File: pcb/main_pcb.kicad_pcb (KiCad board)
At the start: 2 copper layers, 62 x 67 mm, 30 parts, among them J1 Conn_01x06_Socket, J2 Conn_01x10_Pin, J3 Conn_01x06_Pin, J4 USB_C_Receptacle_USB2.0, SW1 SW_Push, SW2 SW_Push, SW3 SW_Push, U1 ESP32-H2-MINI-1, U2 LM5165Y

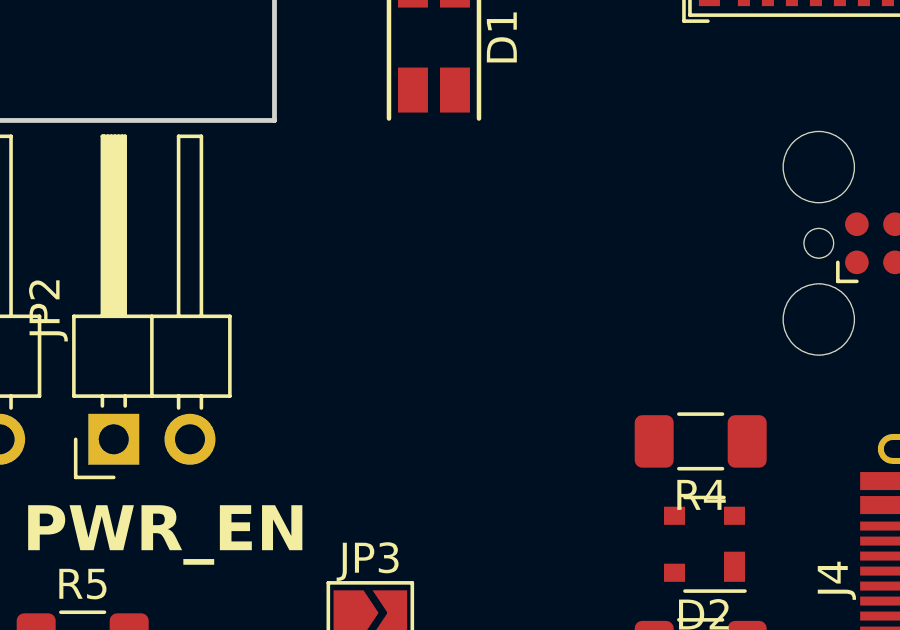
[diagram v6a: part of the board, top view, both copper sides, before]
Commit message: Improve USB circuit
Add reverse voltage protection and VBUS capacitor.
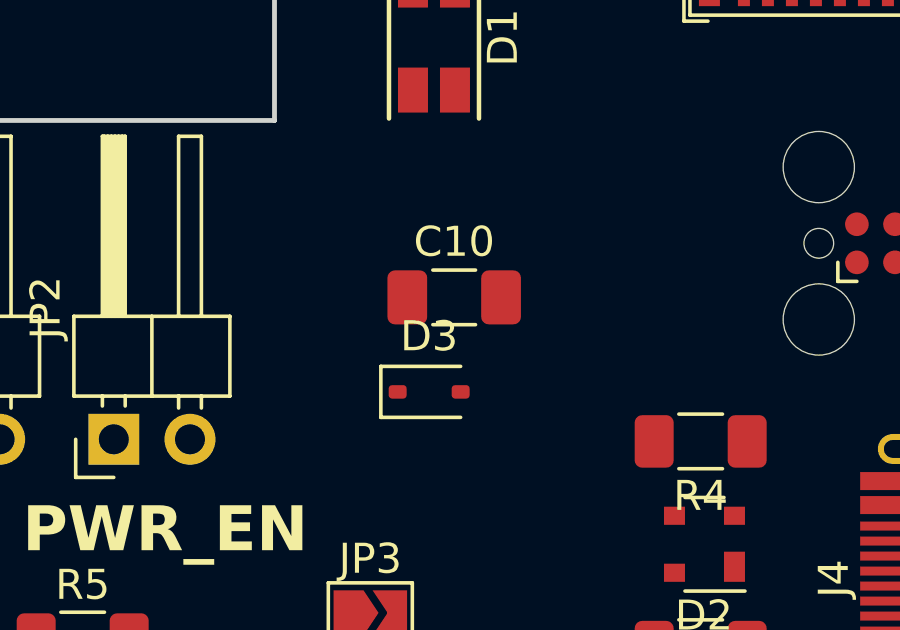
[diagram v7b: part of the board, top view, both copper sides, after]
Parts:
- added C10: 10uF, Capacitor_SMD:C_1206_3216Metric_Pad1.33x1.80mm_HandSolder, F.Cu at (148.5, 70.1)
- added D3: 1N5819WS, Diode_SMD:D_SOD-323, F.Cu at (147.7, 73.3)
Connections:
- JP3 pad 2: VDD -> Net-(D3-A)
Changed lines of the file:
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@@
   (net 59 "unconnected-(U1-GPIO12-Pad16)")
   (net 60 "Net-(R6-Pad2)")
+  (net 61 "unconnected-(C10-Pad2)")
+  (net 62 "Net-(D3-A)")
   (footprint "Button_Switch_SMD:SW_SPST_PTS645" (layer "F.Cu")
     (at 165.227 98.679)
@@
       ))
     (pad "2" smd custom (at 0.725 0) (size 0.3 0.3) (layers "F.Cu" "F.Mask")
-      (net 29 "VDD") (pinfunction "B") (pintype "passive") (zone_connect 2)
+      (net 62 "Net-(D3-A)") (pinfunction "B") (pintype "passive") (zone_connect 2)
       (options (clearance outline) (anchor rect))
       (primitives
@@
   )
   (footprint "Capacitor_SMD:C_1206_3216Metric_Pad1.33x1.80mm_HandSolder" (layer "F.Cu")
+    (at 148.502 70.129)
+    (descr "Capacitor SMD 1206 (3216 Metric), square (rectangular) end terminal, IPC_7351 nominal with elongated pad for handsoldering. (Body size source: IPC-SM-782 page 76, https://www.pcb-3d.com/wordpress/wp-content/uploads/ipc-sm-782a_amendment_1_and_2.pdf), generated with kicad-footprint-generator")
+    (tags "capacitor handsolder")
+    (property "Sheetfile" "main_pcb.kicad_sch")
+    (property "Sheetname" "")
+    (property "ki_description" "Unpolarized capacitor")
+    (property "ki_keywords" "cap capacitor")
+    (attr smd)
+    (fp_text reference "C10" (at 0 -1.85) (layer "F.SilkS")
+        (effects (font (size 1 1) (thickness 0.15)))
+    )
+    (fp_text value "10uF" (at 0 1.85) (layer "F.Fab")
+        (effects (font (size 1 1) (thickness 0.15)))
+    )
+    (fp_text user "${REFERENCE}" (at 0 0) (layer "F.Fab")
+        (effects (font (size 0.8 0.8) (thickness 0.12)))
+    )
+    (fp_line (start -0.711252 -0.91) (end 0.711252 -0.91)
+      (stroke (width 0.12) (type solid)) (layer "F.SilkS"))
+    (fp_line (start -0.711252 0.91) (end 0.711252 0.91)
+      (stroke (width 0.12) (type solid)) (layer "F.SilkS"))
+    (fp_line (start -2.48 -1.15) (end 2.48 -1.15)
+      (stroke (width 0.05) (type solid)) (layer "F.CrtYd"))
+    (fp_line (start -2.48 1.15) (end -2.48 -1.15)
+      (stroke (width 0.05) (type solid)) (layer "F.CrtYd"))
+    (fp_line (start 2.48 -1.15) (end 2.48 1.15)
+      (stroke (width 0.05) (type solid)) (layer "F.CrtYd"))
+    (fp_line (start 2.48 1.15) (end -2.48 1.15)
+      (stroke (width 0.05) (type solid)) (layer "F.CrtYd"))
+    (fp_line (start -1.6 -0.8) (end 1.6 -0.8)
+      (stroke (width 0.1) (type solid)) (layer "F.Fab"))
+    (fp_line (start -1.6 0.8) (end -1.6 -0.8)
+      (stroke (width 0.1) (type solid)) (layer "F.Fab"))
+    (fp_line (start 1.6 -0.8) (end 1.6 0.8)
+      (stroke (width 0.1) (type solid)) (layer "F.Fab"))
+    (fp_line (start 1.6 0.8) (end -1.6 0.8)
+      (stroke (width 0.1) (type solid)) (layer "F.Fab"))
+    (pad "1" smd roundrect (at -1.5625 0) (size 1.325 1.8) (layers "F.Cu" "F.Paste" "F.Mask") (roundrect_rratio 0.188679)
+      (net 29 "VDD") (pintype "passive"))
+    (pad "2" smd roundrect (at 1.5625 0) (size 1.325 1.8) (layers "F.Cu" "F.Paste" "F.Mask") (roundrect_rratio 0.188679)
+      (net 61 "unconnected-(C10-Pad2)") (pintype "passive"))
+    (model "${KICAD6_3DMODEL_DIR}/Capacitor_SMD.3dshapes/C_1206_3216Metric.wrl"
+      (offset (xyz 0 0 0))
+      (scale (xyz 1 1 1))
+      (rotate (xyz 0 0 0))
+    )
+  )
+  (footprint "Capacitor_SMD:C_1206_3216Metric_Pad1.33x1.80mm_HandSolder" (layer "F.Cu")
     (at 130.556 80.264)
     (descr "Capacitor SMD 1206 (3216 Metric), square (rectangular) end terminal, IPC_7351 nominal with elongated pad for handsoldering. (Body size source: IPC-SM-782 page 76, https://www.pcb-3d.com/wordpress/wp-content/uploads/ipc-sm-782a_amendment_1_and_2.pdf), generated with kicad-footprint-generator")
@@
       (offset (xyz 0 0 0))
       (scale (xyz 1 1 1))
+      (rotate (xyz 0 0 0))
+    )
+  )
+  (footprint "Diode_SMD:D_SOD-323" (layer "F.Cu")
+    (at 147.667 73.279)
+    (descr "SOD-323")
+    (tags "SOD-323")
+    (property "Sheetfile" "main_pcb.kicad_sch")
+    (property "Sheetname" "")
+    (property "ki_description" "40V 600mV@1A 1A SOD-323 Schottky Barrier Diodes, SOD-323")
+    (property "ki_keywords" "diode Schottky")
+    (attr smd)
+    (fp_text reference "D3" (at 0 -1.85) (layer "F.SilkS")
+        (effects (font (size 1 1) (thickness 0.15)))
+    )
+    (fp_text value "1N5819WS" (at 0.1 1.9) (layer "F.Fab")
+        (effects (font (size 1 1) (thickness 0.15)))
+    )
+    (fp_text user "${REFERENCE}" (at 0 -1.85) (layer "F.Fab")
+        (effects (font (size 1 1) (thickness 0.15)))
+    )
+    (fp_line (start -1.61 -0.85) (end -1.61 0.85)
+      (stroke (width 0.12) (type solid)) (layer "F.SilkS"))
+    (fp_line (start -1.61 -0.85) (end 1.05 -0.85)
+      (stroke (width 0.12) (type solid)) (layer "F.SilkS"))
+    (fp_line (start -1.61 0.85) (end 1.05 0.85)
+      (stroke (width 0.12) (type solid)) (layer "F.SilkS"))
+    (fp_line (start -1.6 -0.95) (end -1.6 0.95)
+      (stroke (width 0.05) (type solid)) (layer "F.CrtYd"))
+    (fp_line (start -1.6 -0.95) (end 1.6 -0.95)
+      (stroke (width 0.05) (type solid)) (layer "F.CrtYd"))
+    (fp_line (start -1.6 0.95) (end 1.6 0.95)
+      (stroke (width 0.05) (type solid)) (layer "F.CrtYd"))
+    (fp_line (start 1.6 -0.95) (end 1.6 0.95)
+      (stroke (width 0.05) (type solid)) (layer "F.CrtYd"))
+    (fp_line (start -0.9 -0.7) (end 0.9 -0.7)
+      (stroke (width 0.1) (type solid)) (layer "F.Fab"))
+    (fp_line (start -0.9 0.7) (end -0.9 -0.7)
+      (stroke (width 0.1) (type solid)) (layer "F.Fab"))
+    (fp_line (start -0.3 -0.35) (end -0.3 0.35)
+      (stroke (width 0.1) (type solid)) (layer "F.Fab"))
+    (fp_line (start -0.3 0) (end -0.5 0)
+      (stroke (width 0.1) (type solid)) (layer "F.Fab"))
+    (fp_line (start -0.3 0) (end 0.2 -0.35)
+      (stroke (width 0.1) (type solid)) (layer "F.Fab"))
+    (fp_line (start 0.2 -0.35) (end 0.2 0.35)
+      (stroke (width 0.1) (type solid)) (layer "F.Fab"))
+    (fp_line (start 0.2 0) (end 0.45 0)
+      (stroke (width 0.1) (type solid)) (layer "F.Fab"))
+    (fp_line (start 0.2 0.35) (end -0.3 0)
+      (stroke (width 0.1) (type solid)) (layer "F.Fab"))
+    (fp_line (start 0.9 -0.7) (end 0.9 0.7)
+      (stroke (width 0.1) (type solid)) (layer "F.Fab"))
+    (fp_line (start 0.9 0.7) (end -0.9 0.7)
+      (stroke (width 0.1) (type solid)) (layer "F.Fab"))
+    (pad "1" smd roundrect (at -1.05 0) (size 0.6 0.45) (layers "F.Cu" "F.Paste" "F.Mask") (roundrect_rratio 0.25)
+      (net 29 "VDD") (pinfunction "K") (pintype "passive"))
+    (pad "2" smd roundrect (at 1.05 0) (size 0.6 0.45) (layers "F.Cu" "F.Paste" "F.Mask") (roundrect_rratio 0.25)
+      (net 62 "Net-(D3-A)") (pinfunction "A") (pintype "passive"))
+    (model "${KICAD6_3DMODEL_DIR}/Diode_SMD.3dshapes/D_SOD-323.wrl"
+      (offset (xyz 0 0 0))
+      (scale (xyz 1 1 1))

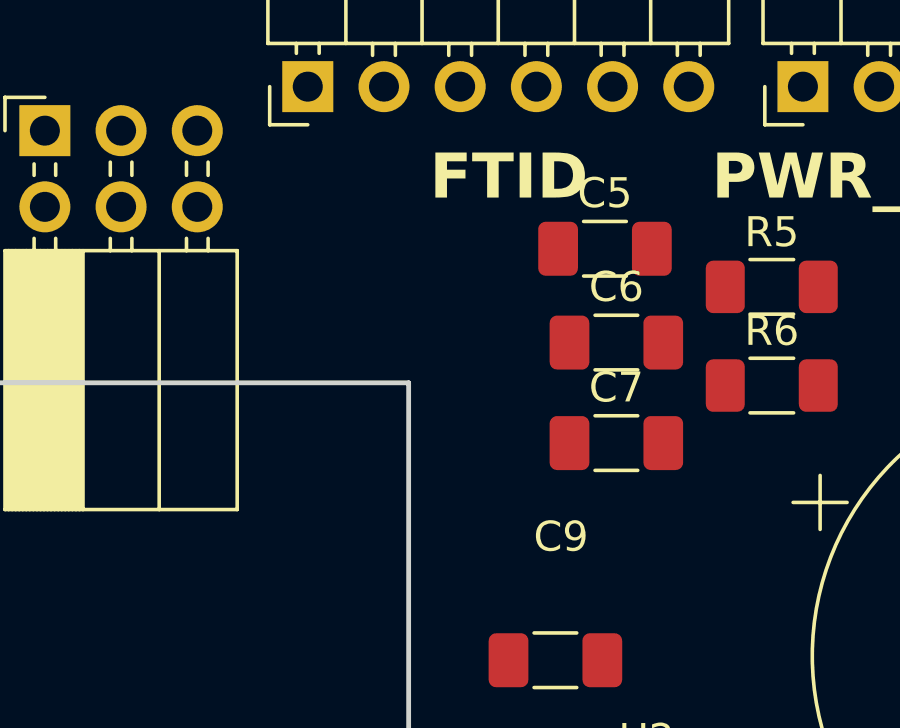
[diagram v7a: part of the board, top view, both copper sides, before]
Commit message: Add reverse current protection to HAN-interface
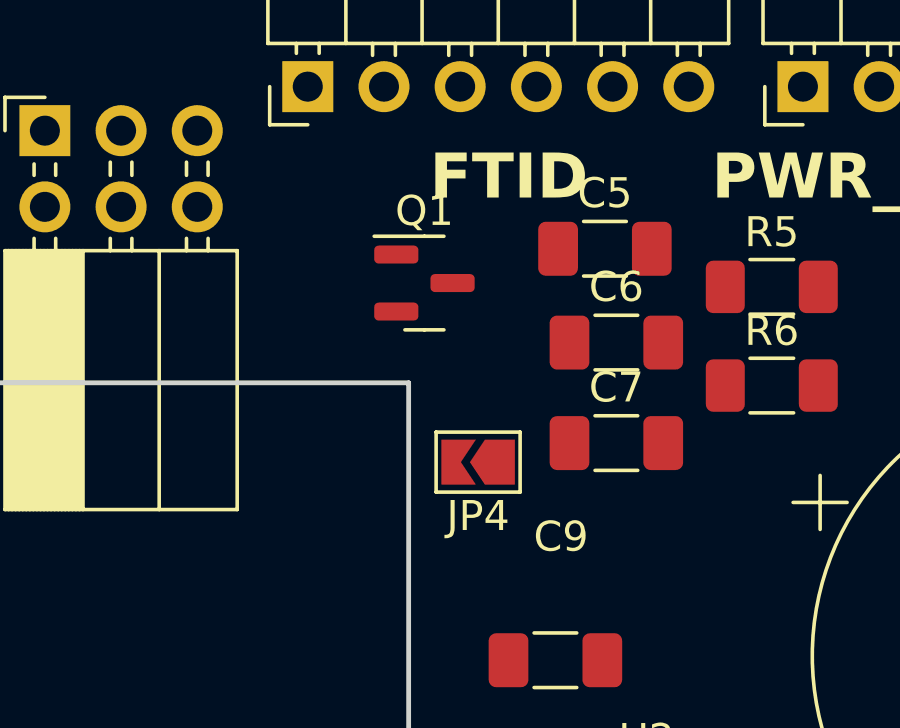
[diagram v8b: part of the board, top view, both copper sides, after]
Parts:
- added JP4: SolderJumper_2_Open, Jumper:SolderJumper-2_P1.3mm_Open_TrianglePad1.0x1.5mm, F.Cu at (126.3, 87.4)
- added Q1: Si2323DS, Package_TO_SOT_SMD:SOT-23, F.Cu at (124.5, 81.4)
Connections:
- J1 pad 1: VDD -> Net-(J1-Pin_1)
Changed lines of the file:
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@@
   (net 61 "unconnected-(C10-Pad2)")
   (net 62 "Net-(D3-A)")
+  (net 63 "Net-(J1-Pin_1)")
   (footprint "Button_Switch_SMD:SW_SPST_PTS645" (layer "F.Cu")
     (at 165.227 98.679)
@@
       (net 32 "GND") (pintype "passive"))
     (model "${KICAD6_3DMODEL_DIR}/Capacitor_SMD.3dshapes/C_1206_3216Metric.wrl"
+      (offset (xyz 0 0 0))
+      (scale (xyz 1 1 1))
+      (rotate (xyz 0 0 0))
+    )
+  )
+  (footprint "Package_TO_SOT_SMD:SOT-23" (layer "F.Cu")
+    (at 124.5385 81.407)
+    (descr "SOT, 3 Pin (https://www.jedec.org/system/files/docs/to-236h.pdf variant AB), generated with kicad-footprint-generator ipc_gullwing_generator.py")
+    (tags "SOT TO_SOT_SMD")
+    (property "Sheetfile" "main_pcb.kicad_sch")
+    (property "Sheetname" "")
+    (property "ki_description" "3.7A Id, 20V Vds, P-Channel MOSFET, SOT-23")
+    (property "ki_keywords" "P-Channel MOSFET")
+    (attr smd)
+    (fp_text reference "Q1" (at 0 -2.4) (layer "F.SilkS")
+        (effects (font (size 1 1) (thickness 0.15)))
+    )
+    (fp_text value "Si2323DS" (at 0 2.4) (layer "F.Fab")
+        (effects (font (size 1 1) (thickness 0.15)))
+    )
+    (fp_text user "${REFERENCE}" (at 0 0) (layer "F.Fab")
+        (effects (font (size 0.32 0.32) (thickness 0.05)))
+    )
+    (fp_line (start 0 -1.56) (end -1.675 -1.56)
+      (stroke (width 0.12) (type solid)) (layer "F.SilkS"))
+    (fp_line (start 0 -1.56) (end 0.65 -1.56)
+      (stroke (width 0.12) (type solid)) (layer "F.SilkS"))
+    (fp_line (start 0 1.56) (end -0.65 1.56)
+      (stroke (width 0.12) (type solid)) (layer "F.SilkS"))
+    (fp_line (start 0 1.56) (end 0.65 1.56)
+      (stroke (width 0.12) (type solid)) (layer "F.SilkS"))
+    (fp_line (start -1.92 -1.7) (end -1.92 1.7)
+      (stroke (width 0.05) (type solid)) (layer "F.CrtYd"))
+    (fp_line (start -1.92 1.7) (end 1.92 1.7)
+      (stroke (width 0.05) (type solid)) (layer "F.CrtYd"))
+    (fp_line (start 1.92 -1.7) (end -1.92 -1.7)
+      (stroke (width 0.05) (type solid)) (layer "F.CrtYd"))
+    (fp_line (start 1.92 1.7) (end 1.92 -1.7)
+      (stroke (width 0.05) (type solid)) (layer "F.CrtYd"))
+    (fp_line (start -0.65 -1.125) (end -0.325 -1.45)
+      (stroke (width 0.1) (type solid)) (layer "F.Fab"))
+    (fp_line (start -0.65 1.45) (end -0.65 -1.125)
+      (stroke (width 0.1) (type solid)) (layer "F.Fab"))
+    (fp_line (start -0.325 -1.45) (end 0.65 -1.45)
+      (stroke (width 0.1) (type solid)) (layer "F.Fab"))
+    (fp_line (start 0.65 -1.45) (end 0.65 1.45)
+      (stroke (width 0.1) (type solid)) (layer "F.Fab"))
+    (fp_line (start 0.65 1.45) (end -0.65 1.45)
+      (stroke (width 0.1) (type solid)) (layer "F.Fab"))
+    (pad "1" smd roundrect (at -0.9375 -0.95) (size 1.475 0.6) (layers "F.Cu" "F.Paste" "F.Mask") (roundrect_rratio 0.25)
+      (net 32 "GND") (pinfunction "G") (pintype "input"))
+    (pad "2" smd roundrect (at -0.9375 0.95) (size 1.475 0.6) (layers "F.Cu" "F.Paste" "F.Mask") (roundrect_rratio 0.25)
+      (net 29 "VDD") (pinfunction "S") (pintype "passive"))
+    (pad "3" smd roundrect (at 0.9375 0) (size 1.475 0.6) (layers "F.Cu" "F.Paste" "F.Mask") (roundrect_rratio 0.25)
+      (net 63 "Net-(J1-Pin_1)") (pinfunction "D") (pintype "passive"))
+    (model "${KICAD6_3DMODEL_DIR}/Package_TO_SOT_SMD.3dshapes/SOT-23.wrl"
       (offset (xyz 0 0 0))
       (scale (xyz 1 1 1))
@@
         (effects (font (size 1 1) (thickness 0.15)))
     )
-    (fp_text value "1uF" (at -28.321 1.596) (layer "F.Fab")
-        (effects (font (size 1 1) (thickness 0.15)))
-    )
-    (fp_text user "${REFERENCE}" (at -28.321 -0.254) (layer "F.Fab")
+    (fp_text value "1uF" (at 3.683 -0.889) (layer "F.Fab")
+        (effects (font (size 1 1) (thickness 0.15)))
+    )
+    (fp_text user "${REFERENCE}" (at 1.6 0.8) (layer "F.Fab")
         (effects (font (size 0.8 0.8) (thickness 0.12)))
     )
@@
     )
   )
+  (footprint "Jumper:SolderJumper-2_P1.3mm_Open_TrianglePad1.0x1.5mm" (layer "F.Cu")
+    (at 126.328 87.376 180)
+    (descr "SMD Solder Jumper, 1x1.5mm Triangular Pads, 0.3mm gap, open")
+    (tags "solder jumper open")
+    (property "Sheetfile" "main_pcb.kicad_sch")
+    (property "Sheetname" "")
+    (property "ki_description" "Solder Jumper, 2-pole, open")
+    (property "ki_keywords" "solder jumper SPST")
+    (attr exclude_from_pos_files)
+    (fp_text reference "JP4" (at 0 -1.8) (layer "F.SilkS")
+        (effects (font (size 1 1) (thickness 0.15)))
+    )
+    (fp_text value "SolderJumper_2_Open" (at 0 1.9) (layer "F.Fab")
+        (effects (font (size 1 1) (thickness 0.15)))
+    )
+    (fp_line (start -1.4 -1) (end 1.4 -1)
+      (stroke (width 0.12) (type solid)) (layer "F.SilkS"))
+    (fp_line (start -1.4 1) (end -1.4 -1)
+      (stroke (width 0.12) (type solid)) (layer "F.SilkS"))
+    (fp_line (start 1.4 -1) (end 1.4 1)
+      (stroke (width 0.12) (type solid)) (layer "F.SilkS"))
+    (fp_line (start 1.4 1) (end -1.4 1)
+      (stroke (width 0.12) (type solid)) (layer "F.SilkS"))
+    (fp_line (start -1.65 -1.25) (end -1.65 1.25)
+      (stroke (width 0.05) (type solid)) (layer "F.CrtYd"))
+    (fp_line (start -1.65 -1.25) (end 1.65 -1.25)
+      (stroke (width 0.05) (type solid)) (layer "F.CrtYd"))
+    (fp_line (start 1.65 1.25) (end -1.65 1.25)
+      (stroke (width 0.05) (type solid)) (layer "F.CrtYd"))
+    (fp_line (start 1.65 1.25) (end 1.65 -1.25)
+      (stroke (width 0.05) (type solid)) (layer "F.CrtYd"))
+    (pad "1" smd custom (at -0.725 0 180) (size 0.3 0.3) (layers "F.Cu" "F.Mask")
+      (net 63 "Net-(J1-Pin_1)") (pinfunction "A") (pintype "passive") (zone_connect 2)
+      (options (clearance outline) (anchor rect))
+      (primitives
+        (gr_poly
+          (pts
+            (xy 1 0)
+            (xy 0.5 0.75)
+            (xy -0.5 0.75)
+            (xy -0.5 -0.75)
+            (xy 0.5 -0.75)
+          )
+          (width 0) (fill yes))
+      ))
+    (pad "2" smd custom (at 0.725 0 180) (size 0.3 0.3) (layers "F.Cu" "F.Mask")
+      (net 29 "VDD") (pinfunction "B") (pintype "passive") (zone_connect 2)
+      (options (clearance outline) (anchor rect))
+      (primitives
+        (gr_poly
+          (pts
+            (xy 0.5 0.75)
+            (xy -0.65 0.75)
+            (xy -0.15 0)
+            (xy -0.65 -0.75)
+            (xy 0.5 -0.75)
+          )
+          (width 0) (fill yes))
+      ))
+  )
   (footprint "LED_SMD:LED_RGB_1210" (layer "F.Cu")
     (at 147.828 61.468 -90)
@@
       (stroke (width 0.1) (type solid)) (layer "F.Fab"))
     (pad "1" thru_hole rect (at 0 0 90) (size 1.7 1.7) (drill 1) (layers "*.Cu" "*.Mask")
-      (net 29 "VDD") (pinfunction "Pin_1") (pintype "passive"))
+      (net 63 "Net-(J1-Pin_1)") (pinfunction "Pin_1") (pintype "passive"))
     (pad "2" thru_hole oval (at -2.54 0 90) (size 1.7 1.7) (drill 1) (layers "*.Cu" "*.Mask")
       (net 30 "/DATA_IN") (pinfunction "Pin_2") (pintype "passive"))
